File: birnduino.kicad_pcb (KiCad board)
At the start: 2 copper layers, 68.6 x 53.3 mm, 28 parts, among them IC1 ATmega328P, IC2 MAX232, Q1 16 MHz, SW1 RESET, U4 78L33, U5 LM7805

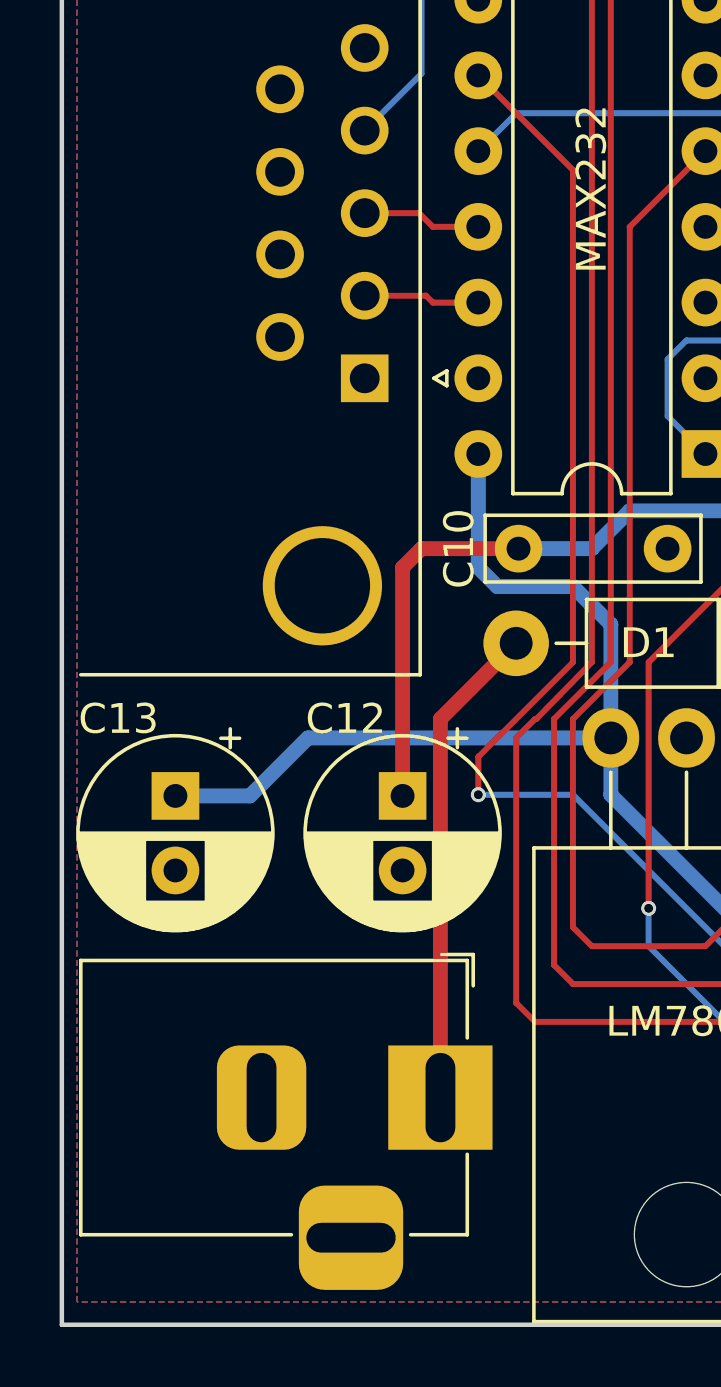
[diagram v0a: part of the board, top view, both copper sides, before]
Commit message: Update of board/library to change D-SUB connector and power jack.
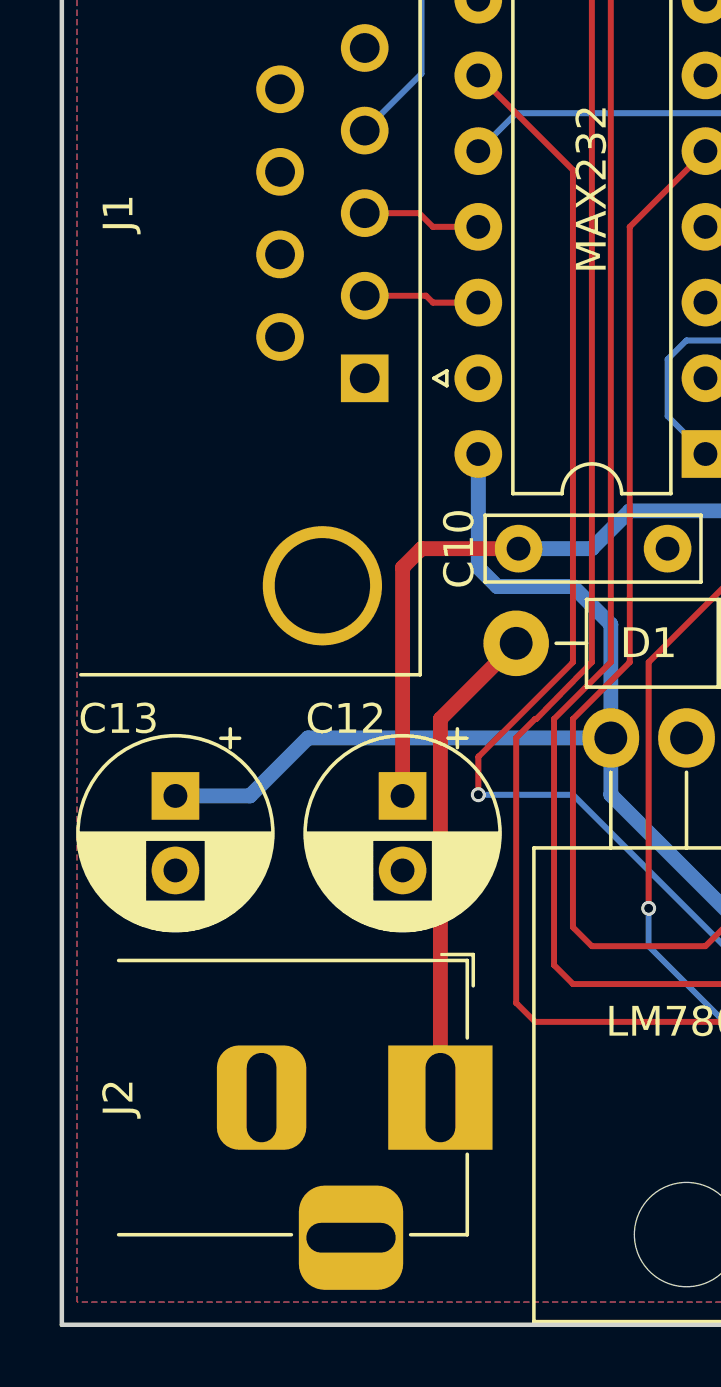
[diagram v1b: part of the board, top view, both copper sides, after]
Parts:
- added J1: RS232, Connector_Dsub:DSUB-9_Female_Horizontal_P2.77x2.84mm_EdgePinOffset7.70mm_Housed_MountingHolesOffset9.12mm, F.Cu at (148.6, 71.1)
- added J2: Power, Connector_BarrelJack:BarrelJack_Horizontal, F.Cu at (151.1, 95.2)
- XA1: value Arduino_Serial_Shield -> Arduino_Serial_Board

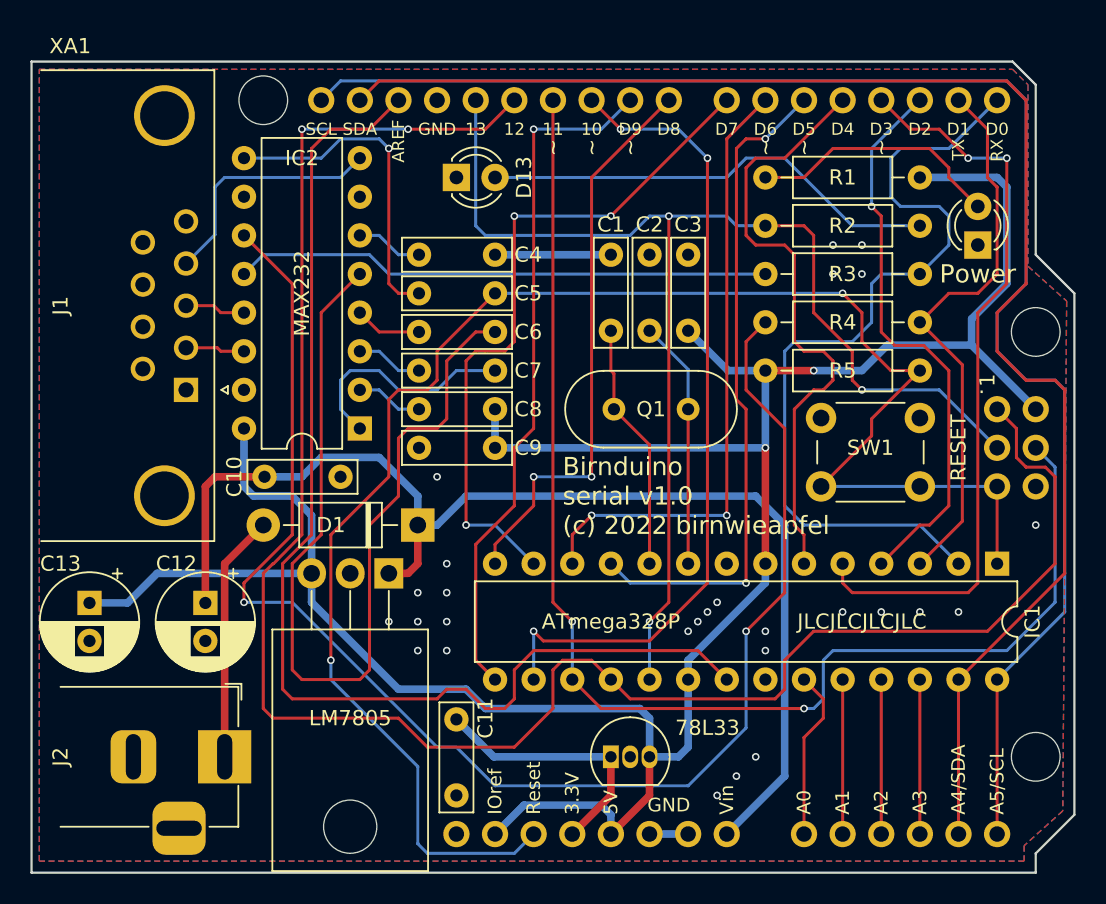
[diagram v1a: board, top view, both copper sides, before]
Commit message: Removed dependencies to Arduino KiCad Library
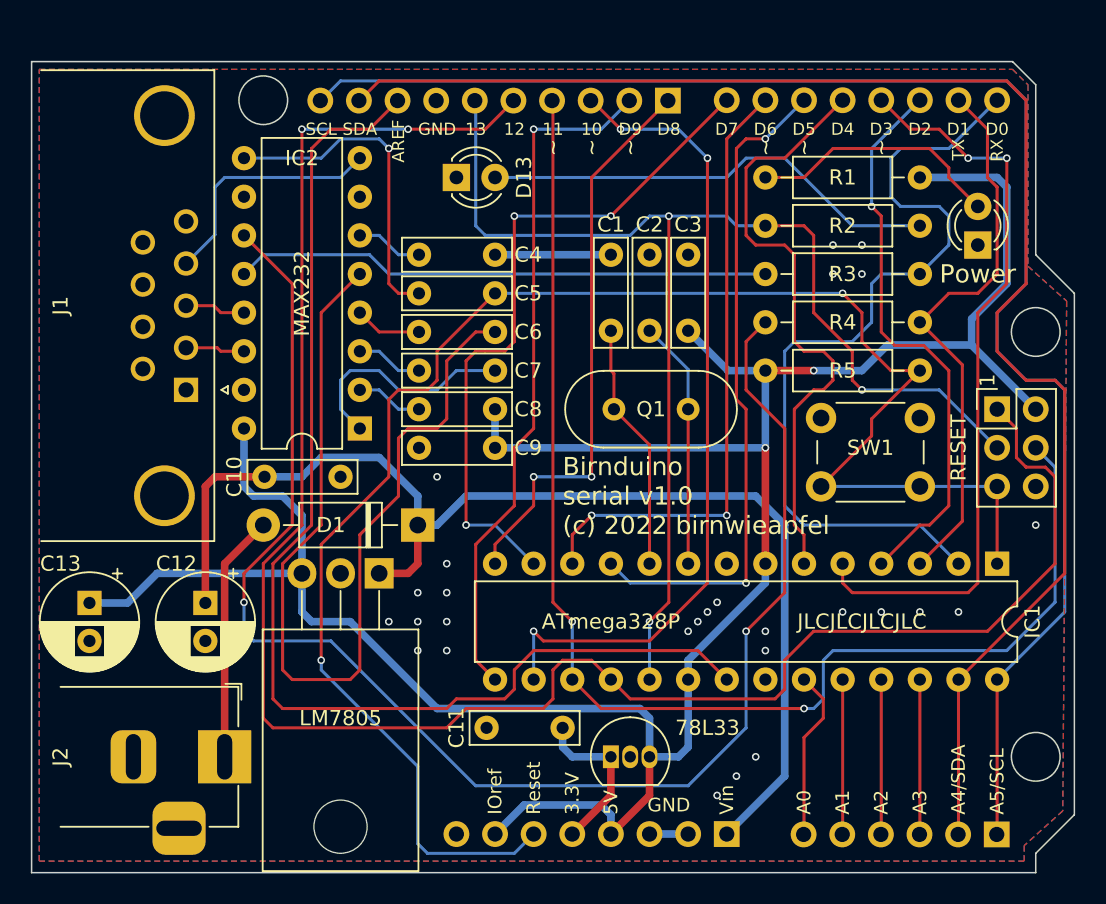
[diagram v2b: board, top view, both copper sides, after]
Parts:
- removed XA1: Arduino_Serial_Board, Arduino:Arduino_Serial_Shield
- added J3: Analog in, Connector_PinSocket_2.54mm:PinSocket_1x06_P2.54mm_Vertical, F.Cu at (201.9, 100.4)
- added J4: Power, Connector_PinSocket_2.54mm:PinSocket_1x08_P2.54mm_Vertical, F.Cu at (184.2, 100.3)
- added J5: Digital_0_7, Connector_PinSocket_2.54mm:PinSocket_1x08_P2.54mm_Vertical, F.Cu at (201.9, 52.1)
- added J6: Digital_8_13, Connector_PinSocket_2.54mm:PinSocket_1x10_P2.54mm_Vertical, F.Cu at (180.3, 52.1)
- added J7: AVR-ISP-6, Connector_PinHeader_2.54mm:PinHeader_2x03_P2.54mm_Vertical, F.Cu at (201.9, 72.4)
- moved C11 7.01 mm to (173.4, 93.3), turned to 180 degrees
- moved U5 0.64 mm to (161.3, 83.2)
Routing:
- net +3V3: track 17.3 -> 10.8 mm
- net Net-(IC2-Pad11): track 95.7 -> 96.8 mm
- net /D12: track 129.2 -> 128.2 mm
- net /VIN: track 77.7 -> 78.3 mm
- net /RESET: track 110.7 -> 111.2 mm
- net Net-(C6-Pad2): track 61.0 -> 61.5 mm
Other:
- outline, holes or cut-outs redrawn
